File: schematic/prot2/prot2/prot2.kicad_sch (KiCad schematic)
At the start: 22 parts, among them J1 SAFE MODE, J2 Contactor, J3 FCU, J4 Power, J5 Conn_01x06_Pin, J6 Load, SW1 SW_DIP_x01, SW2 SW_Reed, SW3 SW_Reed, U1 STM32F070F6Px

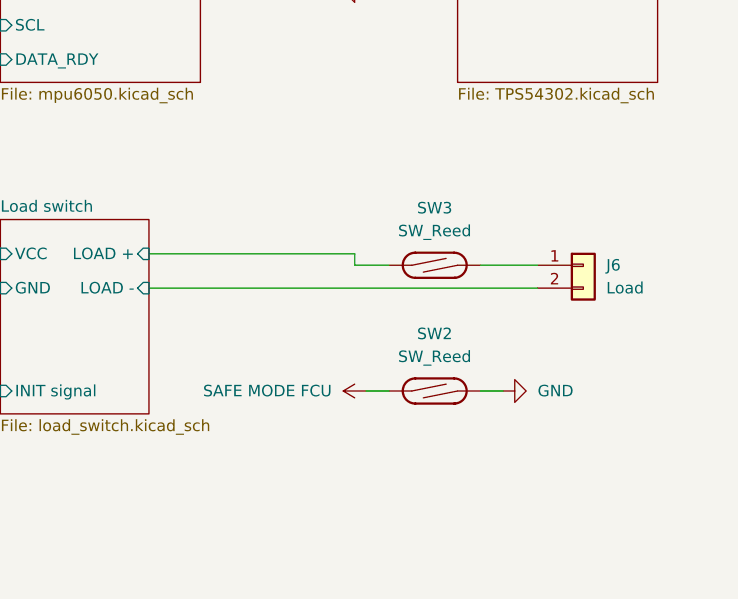
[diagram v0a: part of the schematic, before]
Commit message: Interrupt fix and schematic fix
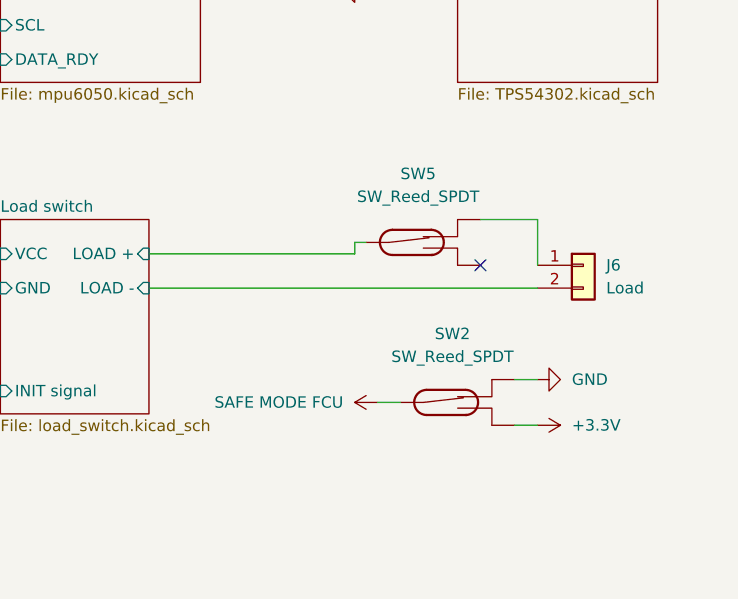
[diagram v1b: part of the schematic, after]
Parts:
- removed SW2, SW3: SW_Reed, symbol Switch:SW_Reed
- added SW2, SW5: SW_Reed_SPDT, symbol Switch:SW_Reed_SPDT
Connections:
- net +3.3V: now also SW2.3
- net GND: now also SW2.1
- net Load switch/LOAD +: now also SW5.2
- net SAFE MODE FCU: now also SW2.2
- net at J6.1 (Pin_1): now also SW5.1
- no-connect marks 0 -> 1

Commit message: schematic changes
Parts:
- removed J5: Conn_01x06_Pin, symbol Connector:Conn_01x06_Pin
- removed SW2, SW5: SW_Reed_SPDT, symbol Switch:SW_Reed_SPDT
- added J7: AudioJack4_SwitchTR1, symbol Connector_Audio:AudioJack4_SwitchTR1
- added TP1: TX, TestPoint:TestPoint_Pad_D3.0mm, symbol Connector:TestPoint
- added TP2: RX, TestPoint:TestPoint_Pad_D3.0mm, symbol Connector:TestPoint
- added TP3: SWCLK, TestPoint:TestPoint_Pad_D3.0mm, symbol Connector:TestPoint
- added TP4: SWDIO, TestPoint:TestPoint_Pad_D3.0mm, symbol Connector:TestPoint
- added TP5: 3.3V, TestPoint:TestPoint_Pad_D3.0mm, symbol Connector:TestPoint
- added TP6: GND, TestPoint:TestPoint_Pad_D3.0mm, symbol Connector:TestPoint
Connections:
- net +3.3V: now also TP5.1
- net GND: now also J7.TN, TP6.1
- net Load switch/LOAD +: now also J6.1 (Pin_1)
- net Load switch/LOAD -: now also J7.R1N; no longer J6.2 (Pin_2)
- net RX: now also TP2.1
- net SAFE MODE HARD: now also J7.T
- net SWCLK: now also TP3.1
- net SWDIO: now also TP4.1
- net TX: now also TP1.1
- new net: J6.2 (Pin_2), J7.R1
- no-connect marks 1 -> 2
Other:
- moved on the sheet: J6
